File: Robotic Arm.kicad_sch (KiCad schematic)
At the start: 8 parts

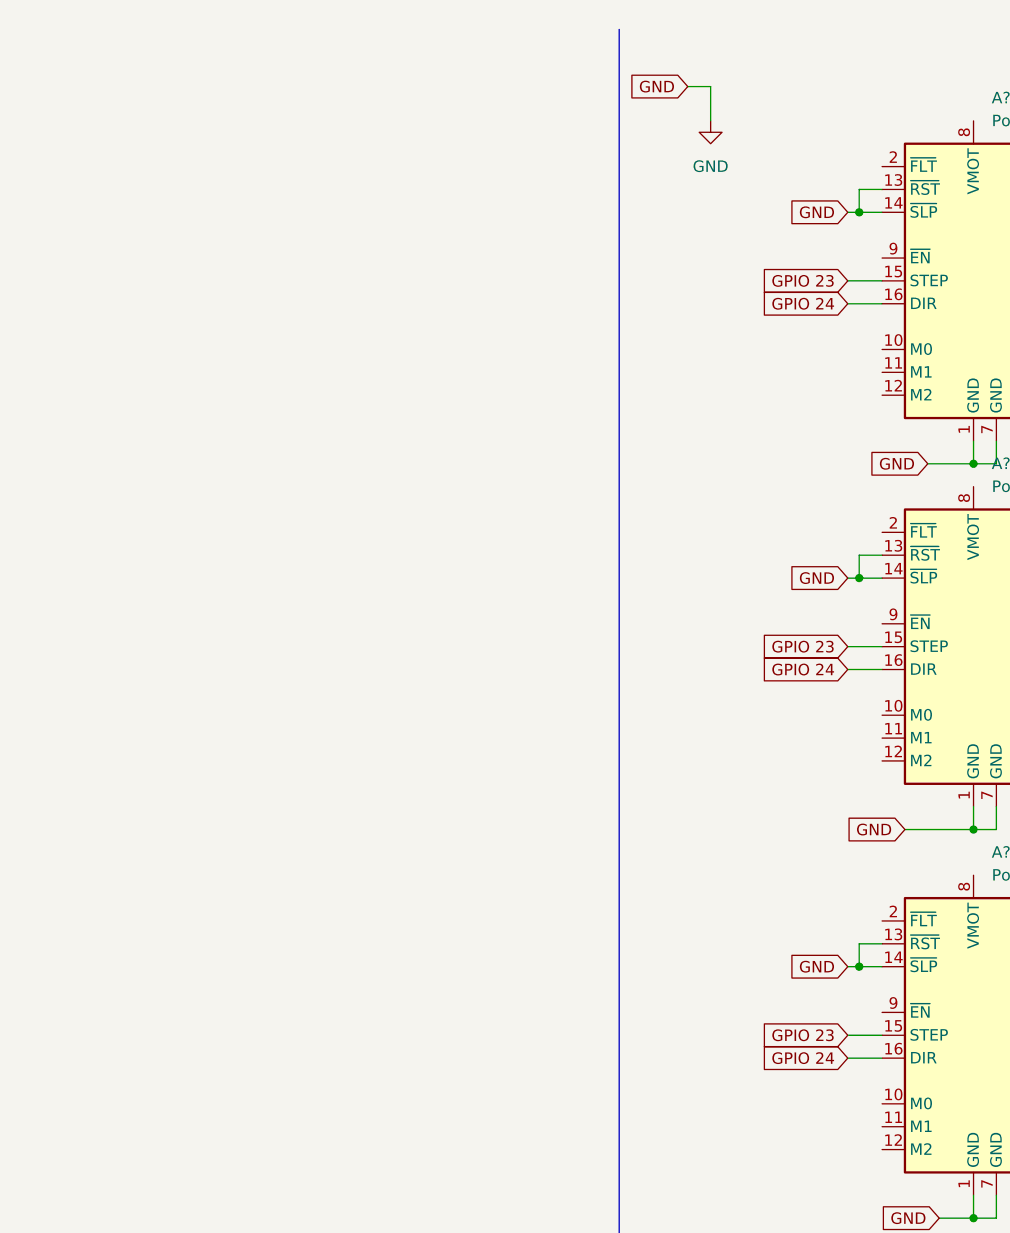
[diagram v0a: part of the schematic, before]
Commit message: pixy2 connectors
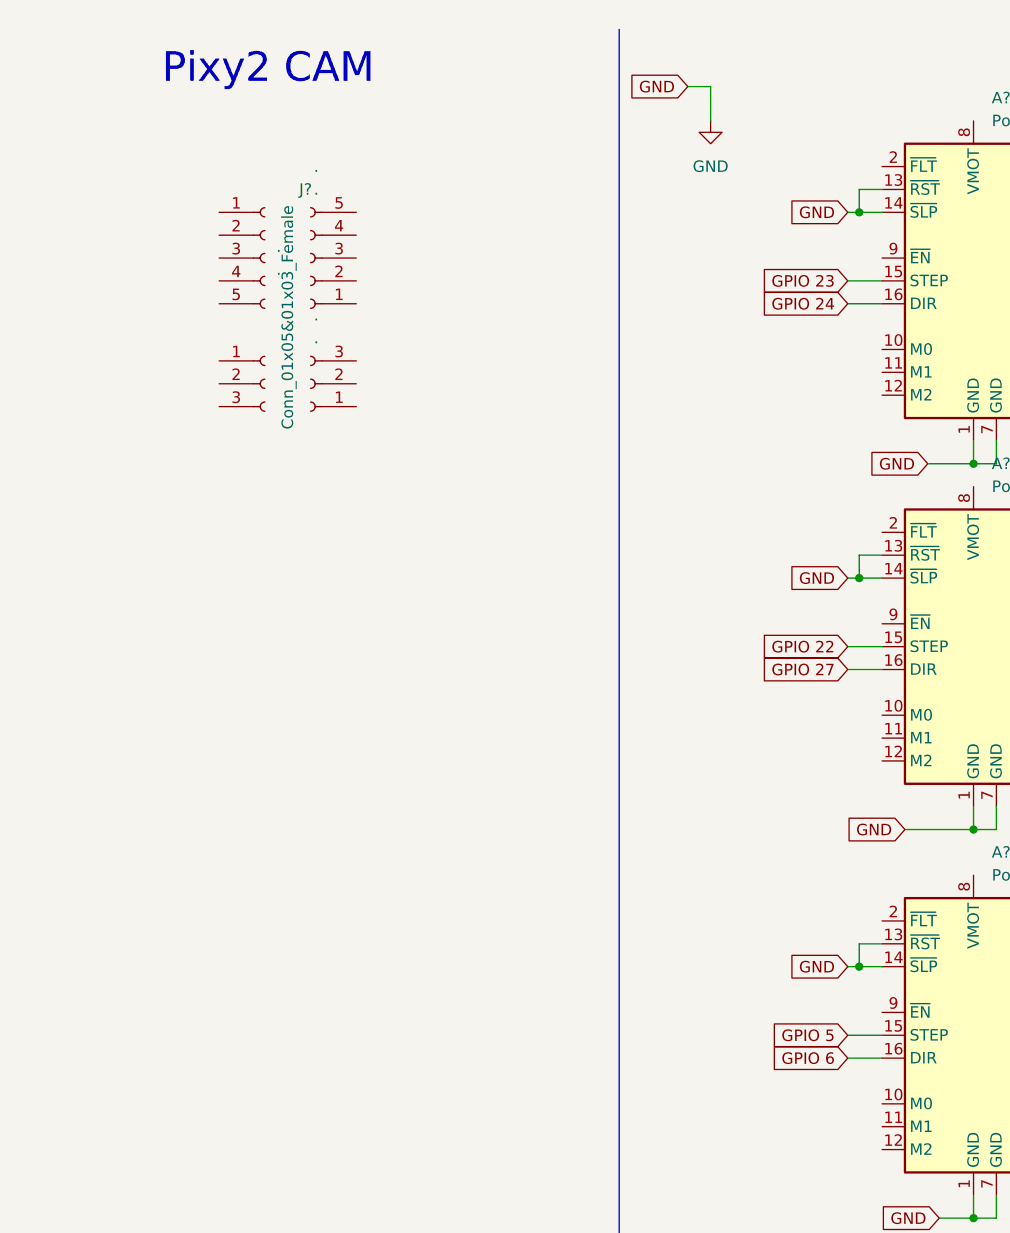
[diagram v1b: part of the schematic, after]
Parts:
- added .: ., symbol Connector:Conn_01x03_Female
- added . (x2): ., symbol Connector:Conn_01x05_Female
- added J?: Conn_01x05&01x03_Female, symbol Connector:Conn_01x03_Female
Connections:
- net GPIO 22: now also A?.15 (STEP)
- net GPIO 23: no longer A?.15 (STEP), A?.15 (STEP)
- net GPIO 24: no longer A?.16 (DIR), A?.16 (DIR)
- net GPIO 27: now also A?.16 (DIR)
- net GPIO 5: now also A?.15 (STEP)
- net GPIO 6: now also A?.16 (DIR)
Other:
- note added: "Pixy2 CAM"
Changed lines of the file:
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@@
     (stroke (width 0) (type default) (color 0 0 0 0))
+  )
+  (text "Pixy2 CAM" (at 128.27 19.05 0)
+    (effects (font (size 3.27 3.27)) (justify left bottom))
   )
   (text "Motors" (at 227.33 17.78 0)
@@
     )
   )
-  (global_label "GPIO 23" (shape input) (at 204.47 81.28 180) (fields_autoplaced)
-    (effects (font (size 1.27 1.27)) (justify right))
-    (property "Intersheet References" "${INTERSHEET_REFS}" (id 0) (at 194.195 81.3594 0)
+  (global_label "GPIO 22" (shape input) (at 204.47 81.28 180) (fields_autoplaced)
+    (effects (font (size 1.27 1.27)) (justify right))
+    (property "Intersheet References" "${INTERSHEET_REFS}" (id 0) (at 194.195 81.2006 0)
       (effects (font (size 1.27 1.27)) (justify right) hide)
     )
@@
     )
   )
-  (global_label "GPIO 23" (shape input) (at 204.47 124.46 180) (fields_autoplaced)
-    (effects (font (size 1.27 1.27)) (justify right))
-    (property "Intersheet References" "${INTERSHEET_REFS}" (id 0) (at 194.195 124.5394 0)
+  (global_label "GPIO 5" (shape input) (at 204.47 124.46 180) (fields_autoplaced)
+    (effects (font (size 1.27 1.27)) (justify right))
+    (property "Intersheet References" "${INTERSHEET_REFS}" (id 0) (at 195.4045 124.3806 0)
       (effects (font (size 1.27 1.27)) (justify right) hide)
     )
@@
     )
   )
-  (global_label "GPIO 24" (shape input) (at 204.47 83.82 180) (fields_autoplaced)
+  (global_label "GPIO 27" (shape input) (at 204.47 83.82 180) (fields_autoplaced)
     (effects (font (size 1.27 1.27)) (justify right))
     (property "Intersheet References" "${INTERSHEET_REFS}" (id 0) (at 194.195 83.7406 0)
@@
     )
   )
-  (global_label "GPIO 24" (shape input) (at 204.47 127 180) (fields_autoplaced)
-    (effects (font (size 1.27 1.27)) (justify right))
-    (property "Intersheet References" "${INTERSHEET_REFS}" (id 0) (at 194.195 126.9206 0)
+  (global_label "GPIO 6" (shape input) (at 204.47 127 180) (fields_autoplaced)
+    (effects (font (size 1.27 1.27)) (justify right))
+    (property "Intersheet References" "${INTERSHEET_REFS}" (id 0) (at 195.4045 126.9206 0)
       (effects (font (size 1.27 1.27)) (justify right) hide)
     )
@@
       (effects (font (size 1.27 1.27)) (justify right) hide)
     )
+  )
+  (symbol (lib_id "Connector:Conn_01x03_Female") (at 144.78 52.07 180) (unit 1)
+    (in_bom yes) (on_board yes) (fields_autoplaced)
+    (property "Reference" "." (id 0) (at 145.415 44.45 0))
+    (property "Value" "." (id 1) (at 145.415 46.99 0))
+    (property "Footprint" "" (id 2) (at 144.78 52.07 0)
+      (effects (font (size 1.27 1.27)) hide)
+    )
+    (property "Datasheet" "~" (id 3) (at 144.78 52.07 0)
+      (effects (font (size 1.27 1.27)) hide)
+    )
+    (pin "1")
+    (pin "2")
+    (pin "3")
+  )
+  (symbol (lib_id "Connector:Conn_01x05_Female") (at 139.7 38.1 0) (unit 1)
+    (in_bom yes) (on_board yes) (fields_autoplaced)
+    (property "Reference" "." (id 0) (at 140.97 36.8299 0)
+      (effects (font (size 1.27 1.27)) (justify left))
+    )
+    (property "Value" "." (id 1) (at 140.97 39.3699 0)
+      (effects (font (size 1.27 1.27)) (justify left))
+    )
+    (property "Footprint" "" (id 2) (at 139.7 38.1 0)
+      (effects (font (size 1.27 1.27)) hide)
+    )
+    (property "Datasheet" "~" (id 3) (at 139.7 38.1 0)
+      (effects (font (size 1.27 1.27)) hide)
+    )
+    (pin "1")
+    (pin "2")
+    (pin "3")
+    (pin "4")
+    (pin "5")
   )
   (symbol (lib_id "Motor:Stepper_Motor_bipolar") (at 256.54 82.55 0) (unit 1)
@@
     (pin "9")
   )
+  (symbol (lib_id "Connector:Conn_01x03_Female") (at 139.7 52.07 0) (unit 1)
+    (in_bom yes) (on_board yes)
+    (property "Reference" "J?" (id 0) (at 143.51 30.48 0)
+      (effects (font (size 1.27 1.27)) (justify left))
+    )
+    (property "Value" "Conn_01x05&01x03_Female" (id 1) (at 142.24 57.15 90)
+      (effects (font (size 1.27 1.27)) (justify left))
+    )
+    (property "Footprint" "" (id 2) (at 139.7 52.07 0)
+      (effects (font (size 1.27 1.27)) hide)
+    )
+    (property "Datasheet" "~" (id 3) (at 139.7 52.07 0)
+      (effects (font (size 1.27 1.27)) hide)
+    )
+    (pin "1")
+    (pin "2")
+    (pin "3")
+  )
   (symbol (lib_id "Connector:Conn_01x20_Female") (at 60.96 46.99 180) (unit 1)
     (in_bom yes) (on_board yes)
@@
     (pin "4")
   )
+  (symbol (lib_id "Connector:Conn_01x05_Female") (at 144.78 38.1 180) (unit 1)
+    (in_bom yes) (on_board yes) (fields_autoplaced)
+    (property "Reference" "." (id 0) (at 145.415 27.94 0))
+    (property "Value" "." (id 1) (at 145.415 30.48 0))
+    (property "Footprint" "" (id 2) (at 144.78 38.1 0)
+      (effects (font (size 1.27 1.27)) hide)
+    )
+    (property "Datasheet" "~" (id 3) (at 144.78 38.1 0)
+      (effects (font (size 1.27 1.27)) hide)
+    )
+    (pin "1")
+    (pin "2")
+    (pin "3")
+    (pin "4")
+    (pin "5")
+  )
   (sheet_instances
     (path "/" (page "1"))
@@
       (reference "#PWR?") (unit 1) (value "GND") (footprint "")
     )
+    (path "/1a50c510-0c0f-468c-a864-1eafcf4bed0d"
+      (reference ".") (unit 1) (value ".") (footprint "")
+    )
+    (path "/1e45d23d-4cf7-4f8c-ac6e-c5c519ba710d"
+      (reference ".") (unit 1) (value ".") (footprint "")
+    )
+    (path "/f19cddb3-6f0c-4bc4-88be-05a6d5df52ff"
+      (reference ".") (unit 1) (value ".") (footprint "")
+    )
     (path "/2cdaab39-81f1-4593-98a9-4b3ba5375c9d"
       (reference "A?") (unit 1) (value "Pololu_Breakout_DRV8825") (footprint "Module:Pololu_Breakout-16_15.2x20.3mm")
@@
       (reference "J?") (unit 1) (value "Conn_01x20_Female") (footprint "")
     )
+    (path "/aa56df2d-867f-418f-90d8-1293e7cef5a7"
+      (reference "J?") (unit 1) (value "Conn_01x05&01x03_Female") (footprint "")
+    )
     (path "/c894312a-55df-4d9f-9528-7bb742c76d1d"

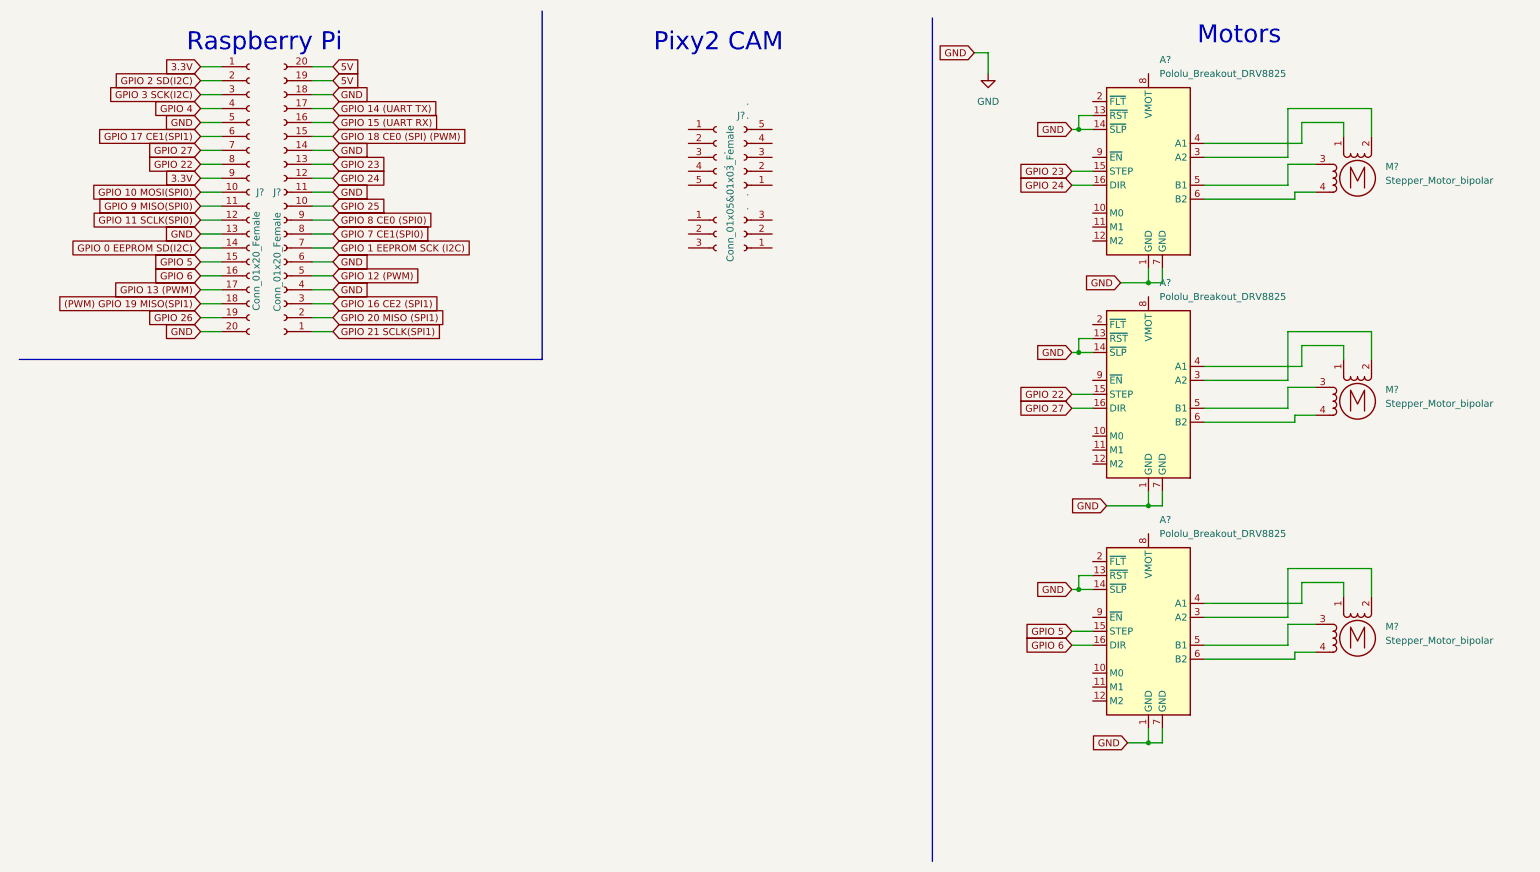
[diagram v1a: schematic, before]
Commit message: Pixy2 Connection to RASPI
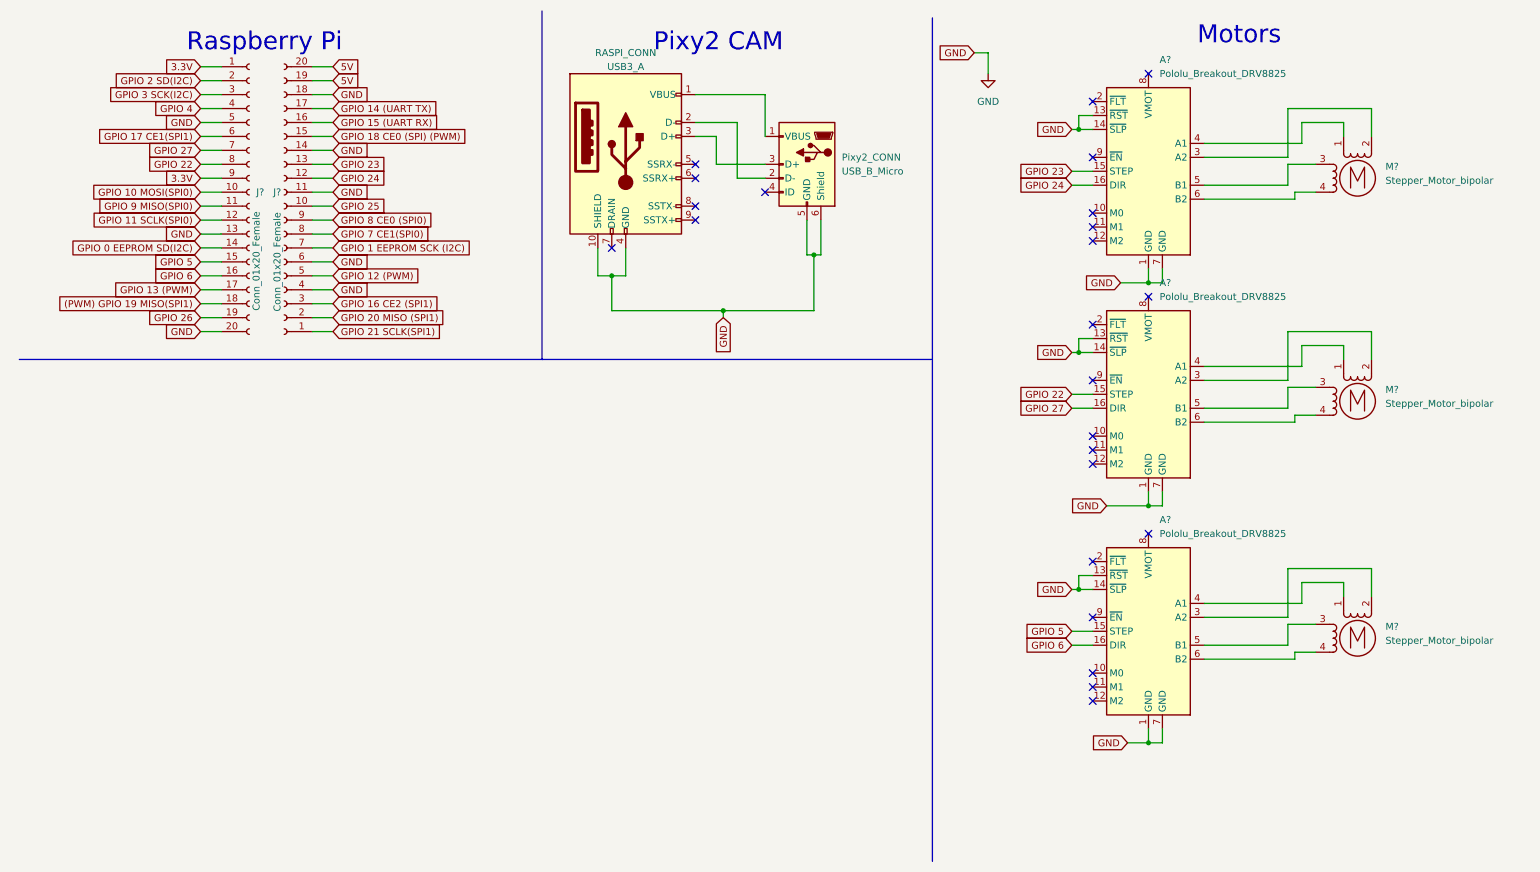
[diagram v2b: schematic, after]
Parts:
- removed .: ., symbol Connector:Conn_01x03_Female
- removed . (x2): ., symbol Connector:Conn_01x05_Female
- removed J?: Conn_01x05&01x03_Female, symbol Connector:Conn_01x03_Female
- added Pixy2_CONN: USB_B_Micro, symbol Connector:USB_B_Micro
- added RASPI_CONN: USB3_A, symbol Connector:USB3_A
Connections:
- net GND: now also Pixy2_CONN.5 (GND), Pixy2_CONN.6 (Shield), RASPI_CONN.10 (SHIELD), RASPI_CONN.4 (GND)
- new net: Pixy2_CONN.1 (VBUS), RASPI_CONN.1 (VBUS)
- new net: Pixy2_CONN.2 (D-), RASPI_CONN.2 (D-)
- new net: Pixy2_CONN.3 (D+), RASPI_CONN.3 (D+)
- no-connect marks 0 -> 24
